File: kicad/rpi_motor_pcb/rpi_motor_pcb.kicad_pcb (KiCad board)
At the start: 2 copper layers, 65 x 84.5 mm, 16 parts, among them J1 Raspberry_Pi_2_3, J10 I2C, J11 LIM_SW, J2 Motor Z1, J3 Motor Z2, J4 PWR IN, J5 Motor X, J6 Motor Y, J7 Motor Z3, J8 I2C, J9 I2C

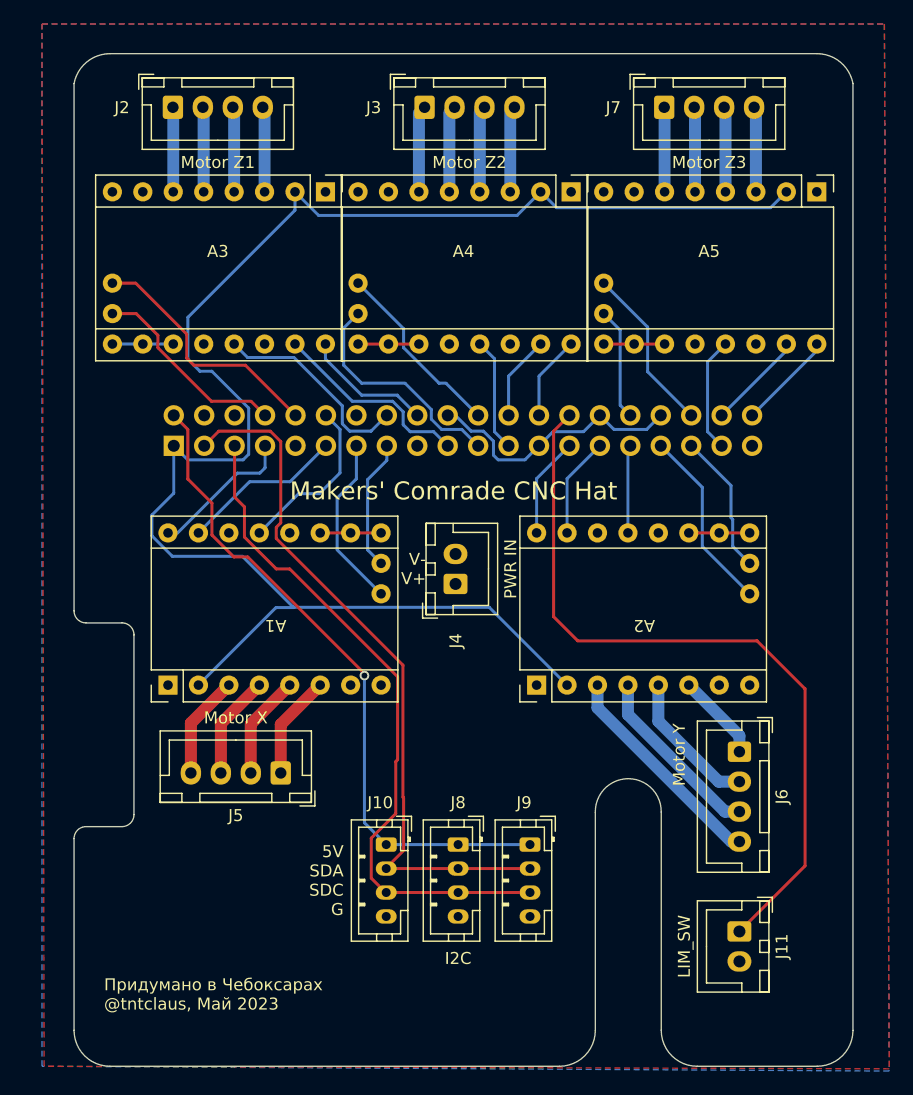
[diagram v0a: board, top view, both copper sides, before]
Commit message: rpi_motor_pcb: 6-axis canbus version
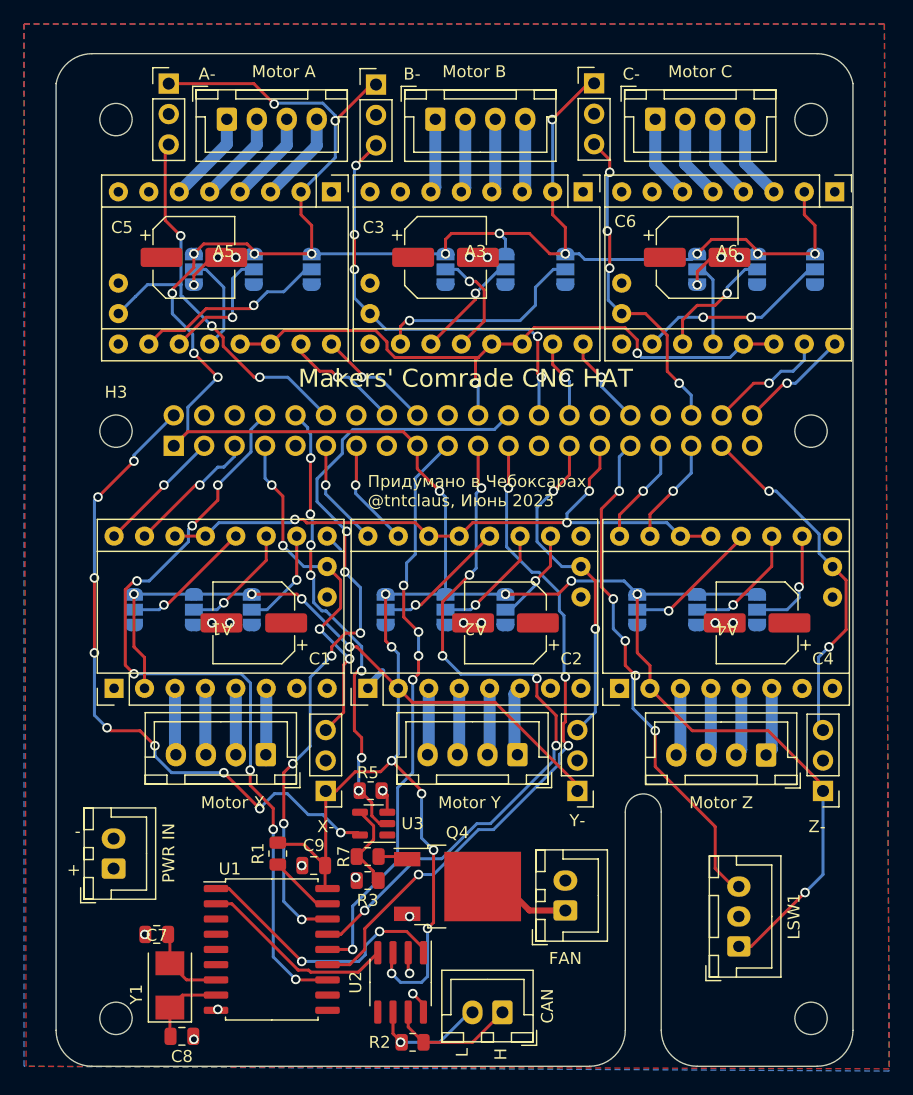
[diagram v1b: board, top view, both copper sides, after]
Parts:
- added A6: Motor C Driver, TMCSockets:TMC220X, F.Cu at (79.0, 33.5)
- added C1: 100µF 50V, Capacitor_SMD:CP_Elec_6.3x7.7, F.Cu at (39.5, 63.0)
- added C2: 100µF 50V, Capacitor_SMD:CP_Elec_6.3x7.7, F.Cu at (60.5, 63.0)
- added C3: 100µF 50V, Capacitor_SMD:CP_Elec_6.3x7.7, F.Cu at (55.5, 32.5)
- added C4: 100µF 50V, Capacitor_SMD:CP_Elec_6.3x7.7, F.Cu at (81.5, 63.0)
- added C5: 100µF 50V, Capacitor_SMD:CP_Elec_6.3x7.7, F.Cu at (34.5, 32.5)
- added C6: 100µF 50V, Capacitor_SMD:CP_Elec_6.3x7.7, F.Cu at (76.5, 32.5)
- added C7: 22pF, Capacitor_SMD:C_0805_2012Metric, F.Cu at (31.4, 89.0)
- added C8: 22pF, Capacitor_SMD:C_0805_2012Metric, F.Cu at (33.5, 97.5)
- added C9: 0.1µF, Capacitor_SMD:C_0805_2012Metric, F.Cu at (44.5, 83.2)
- added H1: MountingHole, MountingHole:MountingHole_2.7mm_M2.5_ISO14580, F.Cu at (28.0, 96.0)
- added H2: MountingHole, MountingHole:MountingHole_2.7mm_M2.5_ISO14580, F.Cu at (86.0, 96.0)
- added H3: MountingHole, MountingHole:MountingHole_2.7mm_M2.5_ISO14580, F.Cu at (28.0, 47.0)
- added H4: MountingHole, MountingHole:MountingHole_2.7mm_M2.5_ISO14580, F.Cu at (86.0, 47.0)
- added H5: MountingHole, MountingHole:MountingHole_2.7mm_M2.5_ISO14580, F.Cu at (28.0, 21.0)
- added H6: MountingHole, MountingHole:MountingHole_2.7mm_M2.5_ISO14580, F.Cu at (86.0, 21.0)
- added J12: Motor C, Connector_JST:JST_XH_B4B-XH-A_1x04_P2.50mm_Vertical, F.Cu at (73.0, 21.0)
- added J13: B-, Connector_PinHeader_2.54mm:PinHeader_1x03_P2.54mm_Vertical, F.Cu at (49.7, 18.1)
- added J14: C-, Connector_PinHeader_2.54mm:PinHeader_1x03_P2.54mm_Vertical, F.Cu at (67.9, 18.0)
- added J15: Y-, Connector_PinHeader_2.54mm:PinHeader_1x03_P2.54mm_Vertical, F.Cu at (66.5, 77.0)
- added J16: Z-, Connector_PinHeader_2.54mm:PinHeader_1x03_P2.54mm_Vertical, F.Cu at (87.0, 77.0)
- added J18: FAN, Connector_JST:JST_XH_B2B-XH-A_1x02_P2.50mm_Vertical, F.Cu at (65.5, 87.0)
- added JP1: MS3, Jumper:SolderJumper-3_P1.3mm_Open_RoundedPad1.0x1.5mm, B.Cu at (29.5, 61.9)
- added JP10: MS3, Jumper:SolderJumper-3_P1.3mm_Open_RoundedPad1.0x1.5mm, B.Cu at (71.5, 61.9)
- added JP11: MS2, Jumper:SolderJumper-3_P1.3mm_Open_RoundedPad1.0x1.5mm, B.Cu at (76.5, 61.9)
- added JP12: MS1, Jumper:SolderJumper-3_P1.3mm_Open_RoundedPad1.0x1.5mm, B.Cu at (81.5, 61.9)
- added JP13: MS3, Jumper:SolderJumper-3_P1.3mm_Open_RoundedPad1.0x1.5mm, B.Cu at (34.5, 33.5)
- added JP14: MS2, Jumper:SolderJumper-3_P1.3mm_Open_RoundedPad1.0x1.5mm, B.Cu at (39.5, 33.5)
- added JP15: MS1, Jumper:SolderJumper-3_P1.3mm_Open_RoundedPad1.0x1.5mm, B.Cu at (44.3, 33.5)
- added JP16: MS3, Jumper:SolderJumper-3_P1.3mm_Open_RoundedPad1.0x1.5mm, B.Cu at (76.5, 33.5)
- added JP17: MS2, Jumper:SolderJumper-3_P1.3mm_Open_RoundedPad1.0x1.5mm, B.Cu at (81.5, 33.5)
- added JP18: MS1, Jumper:SolderJumper-3_P1.3mm_Open_RoundedPad1.0x1.5mm, B.Cu at (86.3, 33.5)
- added JP2: MS2, Jumper:SolderJumper-3_P1.3mm_Open_RoundedPad1.0x1.5mm, B.Cu at (34.5, 61.9)
- added JP3: MS1, Jumper:SolderJumper-3_P1.3mm_Open_RoundedPad1.0x1.5mm, B.Cu at (39.3, 61.9)
- added JP4: MS3, Jumper:SolderJumper-3_P1.3mm_Open_RoundedPad1.0x1.5mm, B.Cu at (50.5, 61.9)
- added JP5: MS2, Jumper:SolderJumper-3_P1.3mm_Open_RoundedPad1.0x1.5mm, B.Cu at (55.5, 61.9)
- added JP6: MS1, Jumper:SolderJumper-3_P1.3mm_Open_RoundedPad1.0x1.5mm, B.Cu at (60.5, 61.9)
- added JP7: MS3, Jumper:SolderJumper-3_P1.3mm_Open_RoundedPad1.0x1.5mm, B.Cu at (55.5, 33.5)
- added JP8: MS2, Jumper:SolderJumper-3_P1.3mm_Open_RoundedPad1.0x1.5mm, B.Cu at (60.5, 33.5)
- added JP9: MS1, Jumper:SolderJumper-3_P1.3mm_Open_RoundedPad1.0x1.5mm, B.Cu at (65.5, 33.5)
- added Q4: HY1403D, Package_TO_SOT_SMD:TO-252-2, F.Cu at (56.5, 85.0)
- added R1: 10k, Resistor_SMD:R_0805_2012Metric, F.Cu at (41.5, 82.2)
- added R2: 120, Resistor_SMD:R_0805_2012Metric, F.Cu at (52.8, 98.0)
- added R3: 10k, Resistor_SMD:R_0805_2012Metric, F.Cu at (49.0, 84.5)
- added R5: 10k, Resistor_SMD:R_0805_2012Metric, F.Cu at (49.2, 77.0)
- added R7: 10k, Resistor_SMD:R_0805_2012Metric, F.Cu at (49.0, 82.5)
- added U1: MCP2515-xSO, Package_SO:SOIC-18W_7.5x11.6mm_P1.27mm, F.Cu at (41.0, 90.2)
- added U2: SN65HVD230, Package_SO:SOIC-8_3.9x4.9mm_P1.27mm, F.Cu at (51.8, 93.0)
- added U3: 74LVC1G17, Package_TO_SOT_SMD:SOT-23-5, F.Cu at (49.5, 79.8)
- added Y1: Crystal, Crystal:Crystal_SMD_5032-2Pin_5.0x3.2mm, F.Cu at (32.5, 93.2)
- A1: value MKS_TMC2209 Motor X -> Motor X Driver
- A2: value MKS_TMC2209 Motor Y -> Motor Y Driver
- A3: value MKS_TMC2209 Motor Z1 -> Motor B Driver
- A4: value MKS_TMC2209 Motor Z2 -> Motor Z Driver
- A5: value MKS_TMC2209 Motor Z3 -> Motor A Driver
- J10: value I2C -> CAN; footprint Connector_JST:JST_PH_B4B-PH-K_1x04_P2.00mm_Vertical -> Connector_JST:JST_XH_B2B-XH-A_1x02_P2.50mm_Vertical
- J11: value LIM_SW -> A-; footprint Connector_JST:JST_XH_B2B-XH-A_1x02_P2.50mm_Vertical -> Connector_PinHeader_2.54mm:PinHeader_1x03_P2.54mm_Vertical
- J2: value Motor Z1 -> Motor Y
- J3: value Motor Z2 -> Motor B
- J6: value Motor Y -> Motor Z
- J7: value Motor Z3 -> Motor A
- J8: value I2C -> X-; footprint Connector_JST:JST_PH_B4B-PH-K_1x04_P2.00mm_Vertical -> Connector_PinHeader_2.54mm:PinHeader_1x03_P2.54mm_Vertical
- J9: value I2C -> LSW1; footprint Connector_JST:JST_PH_B4B-PH-K_1x04_P2.00mm_Vertical -> Connector_JST:JST_XH_B3B-XH-A_1x03_P2.50mm_Vertical
- moved J11 85.3 mm to (32.4, 18.0), turned to 0 degrees
- moved J2 61.2 mm to (61.5, 74.0), turned to 180 degrees
- moved A5 40.5 mm to (37.0, 33.5)
- moved J4 37.1 mm to (27.8, 83.5)
- moved J7 36.5 mm to (37.2, 21.0)
- moved A4 36.0 mm to (79.0, 62.0), turned to 90 degrees
- moved A3 21.5 mm to (58.0, 33.5)
- moved J9 19.4 mm to (80.0, 90.0), turned to 90 degrees
- moved J10 17.0 mm to (60.2, 95.5), turned to 180 degrees
- moved A2 14.1 mm to (58.0, 62.0)
- moved J8 11.9 mm to (45.5, 77.0), turned to 180 degrees
- moved A1 4.51 mm to (36.8, 62.0)
- moved J6 2.24 mm to (82.2, 74.0), turned to 180 degrees
- moved J5 1.97 mm to (40.5, 74.0)
- moved J3 1.35 mm to (54.6, 21.0)
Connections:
- net /Motor Z3/1A renamed /Motor A/1A
- net /Motor Z3/1B renamed /Motor A/1B
- net /Motor Z3/2A renamed /Motor A/2A
- net /Motor Z3/2B renamed /Motor A/2B
- A1 pad 10: GND -> /Motor X/MS1
- A1 pad 11: GND -> /Motor X/MS2
- A1 pad 12: unconnected-(A1-Pad12) -> /Motor X/MS3
- A1 pad 13: /MotX UART -> /UART_X
- A1 pad 14: unconnected-(A1-Pad14) -> /UART_X
- A1 pad 15: /MotX STEP -> /MX STEP
- A1 pad 16: /MotX DIR -> /MX DIR
- A1 pad 17: /MotX DIAG -> /MX DIAG
- A1 pad 18: /MotX INDEX -> unconnected-(A1-Pad18)
- A2 pad 10: GND -> /Motor Y/MS1
- A2 pad 11: GND -> /Motor Y/MS2
- A2 pad 12: unconnected-(A2-Pad12) -> /Motor Y/MS3
- A2 pad 13: /MotY UART -> /UART_X
- A2 pad 14: unconnected-(A2-Pad14) -> /UART_X
- A2 pad 15: /MotY STEP -> /MY STEP
- A2 pad 16: /MotY DIR -> /MY DIR
- A2 pad 17: /MotY DIAG -> /MY DIAG
- A2 pad 18: /MotY INDEX -> unconnected-(A2-Pad18)
- A3 pad 10: GND -> /Motor B/MS1
- A3 pad 11: GND -> /Motor B/MS2
- A3 pad 12: unconnected-(A3-Pad12) -> /Motor B/MS3
- A3 pad 13: /MotZ1 UART -> /UART_A
- A3 pad 14: unconnected-(A3-Pad14) -> /UART_A
- A3 pad 15: /MotZ1 STEP -> /MB STEP
- A3 pad 16: /MotZ1 DIR -> /MB DIR
- A3 pad 17: /MotZ1 DIAG -> /MB DIAG
- A3 pad 18: /MotZ1 INDEX -> unconnected-(A3-Pad18)
- A3 pad 3: /Motor Z1/1B -> /Motor B/1B
- A3 pad 4: /Motor Z1/1A -> /Motor B/1A
- A3 pad 5: /Motor Z1/2A -> /Motor B/2A
- A3 pad 6: /Motor Z1/2B -> /Motor B/2B
- A4 pad 10: GND -> /Motor Z/MS1
- A4 pad 11: GND -> /Motor Z/MS2
- A4 pad 12: unconnected-(A4-Pad12) -> /Motor Z/MS3
- A4 pad 13: /MotZ2 UART -> /UART_X
- A4 pad 14: unconnected-(A4-Pad14) -> /UART_X
- A4 pad 15: /MotZ2 STEP -> /MZ STEP
- A4 pad 16: /MotZ2 DIR -> /MZ DIR
- A4 pad 17: /MotZ2 DIAG -> /MZ DIAG
- A4 pad 18: /MotZ2 INDEX -> unconnected-(A4-Pad18)
- A4 pad 3: /Motor Z2/1B -> /Motor Z/1B
- A4 pad 4: /Motor Z2/1A -> /Motor Z/1A
- A4 pad 5: /Motor Z2/2A -> /Motor Z/2A
- A4 pad 6: /Motor Z2/2B -> /Motor Z/2B
- A5 pad 10: GND -> /Motor A/MS1
- A5 pad 11: GND -> /Motor A/MS2
- A5 pad 12: unconnected-(A5-Pad12) -> /Motor A/MS3
- A5 pad 13: /MotZ3 UART -> /UART_A
- A5 pad 14: unconnected-(A5-Pad14) -> /UART_A
- A5 pad 15: /MotZ3 STEP -> /MA STEP
- A5 pad 16: /MotZ3 DIR -> /MA DIR
- A5 pad 17: /MotZ3 DIAG -> /MA DIAG
- A5 pad 18: /MotZ3 INDEX -> unconnected-(A5-Pad18)
- J1 pad 10: /MotZ1 INDEX -> /FAN
- J1 pad 11: /MotX STEP -> /MY DIR
- J1 pad 12: /MotX UART -> /MA DIAG
- J1 pad 13: /MotX INDEX -> /MY STEP
- J1 pad 15: /MotX DIAG -> unconnected-(J1-Pad15)
- J1 pad 16: /MotZ1 UART -> /MA STEP
- J1 pad 17: unconnected-(J1-Pad17) -> +3V3
- J1 pad 18: /MotZ1 DIR -> /MA DIR
- J1 pad 19: /MotZ1 STEP -> /CAN_MOSI
- J1 pad 2: +5V -> VCC
- J1 pad 21: /MotZ2 DIAG -> /CAN_MISO
- J1 pad 22: /MotZ2 INDEX -> /UART_A
- J1 pad 23: /MotZ2 UART -> /CAN_SCK
- J1 pad 24: /MotZ2 STEP -> /CAN_CS
- J1 pad 26: /MotZ2 DIR -> /MB DIAG
- J1 pad 27: /MotY DIR -> /MY DIAG
- J1 pad 28: /LIM_SW1 -> /MB STEP
- J1 pad 29: /MotY STEP -> /UART_X
- J1 pad 3: /SDA -> /MX DIR
- J1 pad 31: /MotY UART -> /LIM_SW1
- J1 pad 32: /MotZ3 DIAG -> /MB DIR
- J1 pad 33: /MotY INDEX -> /MZ DIR
- J1 pad 35: /MotY DIAG -> /MZ STEP
- J1 pad 36: /MotZ3 INDEX -> /MC DIAG
- J1 pad 37: /MotZ3 UART -> /MZ DIAG
- J1 pad 38: /MotZ3 STEP -> /MC STEP
- J1 pad 40: /MotZ3 DIR -> /MC DIR
- J1 pad 5: /SDC -> /MX STEP
- J1 pad 7: /MotX DIR -> /MX DIAG
- J1 pad 8: /MotZ1 DIAG -> /CAN_INT
- J10 pad 1: +5V -> /CAN/H
- J10 pad 2: /SDA -> /CAN/L
- J11 pad 1: /LIM_SW1 -> +3V3
- J2 pad 1: /Motor Z1/2B -> /Motor Y/2B
- J2 pad 2: /Motor Z1/2A -> /Motor Y/2A
- J2 pad 3: /Motor Z1/1A -> /Motor Y/1A
- J2 pad 4: /Motor Z1/1B -> /Motor Y/1B
- J3 pad 1: /Motor Z2/2B -> /Motor B/2B
- J3 pad 2: /Motor Z2/2A -> /Motor B/2A
- J3 pad 3: /Motor Z2/1A -> /Motor B/1A
- J3 pad 4: /Motor Z2/1B -> /Motor B/1B
- J6 pad 1: /Motor Y/2B -> /Motor Z/2B
- J6 pad 2: /Motor Y/2A -> /Motor Z/2A
- J6 pad 3: /Motor Y/1A -> /Motor Z/1A
- J6 pad 4: /Motor Y/1B -> /Motor Z/1B
- J8 pad 1: +5V -> +3V3
- J8 pad 2: /SDA -> GND
- J8 pad 3: /SDC -> /MX DIAG
- J9 pad 1: +5V -> +3V3
- J9 pad 2: /SDA -> GND
- J9 pad 3: /SDC -> /LIM_SW1
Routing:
- net +3V3: track 137.7 -> 353.6 mm, vias 0 -> 31
- net /CAN_INT: track 0.00 -> 66.5 mm, vias 0 -> 7
- net /CAN_CS: track 0.00 -> 63.4 mm, vias 0 -> 7
- net /CAN_MISO: track 0.00 -> 60.1 mm, vias 0 -> 6
- net /SDA: track 60.0 -> 0.00 mm
- net /SDC: track 57.0 -> 0.00 mm
- net /CAN_SCK: track 0.00 -> 56.9 mm, vias 0 -> 4
- net +5V: track 55.8 -> 0.00 mm, vias 1 -> 0
- net VCC: track 0.00 -> 55.6 mm, vias 0 -> 9
- net /UART_A: track 0.00 -> 54.7 mm, vias 0 -> 2
- net /UART_X: track 0.00 -> 54.4 mm, vias 0 -> 3
- net /CAN_MOSI: track 0.00 -> 48.4 mm, vias 0 -> 5
- net /FAN: track 0.00 -> 38.4 mm, vias 0 -> 7
- net /MB DIAG: track 0.00 -> 36.9 mm, vias 0 -> 5
- net /MA DIAG: track 0.00 -> 36.2 mm, vias 0 -> 3
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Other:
- board size 65 x 84.5 mm -> 66.5 x 84.5 mm
- board text added: "- +"
- board text added: "H"
- board text added: "L"
- board text added: "L H"
- board text added: "Makers' Comrade CNC HAT"
- board text added: "Придумано в Чебоксарах @tntclaus, Июнь 2023"
- board text removed: "5V SDA SDC G"
- board text removed: "Makers' Comrade CNC Hat"
- board text removed: "V- V+"
- board text removed: "Придумано в Чебоксарах @tntclaus, Май 2023"

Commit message: rpi_motor_pcb: 6-axis fix diag pin, add en pin
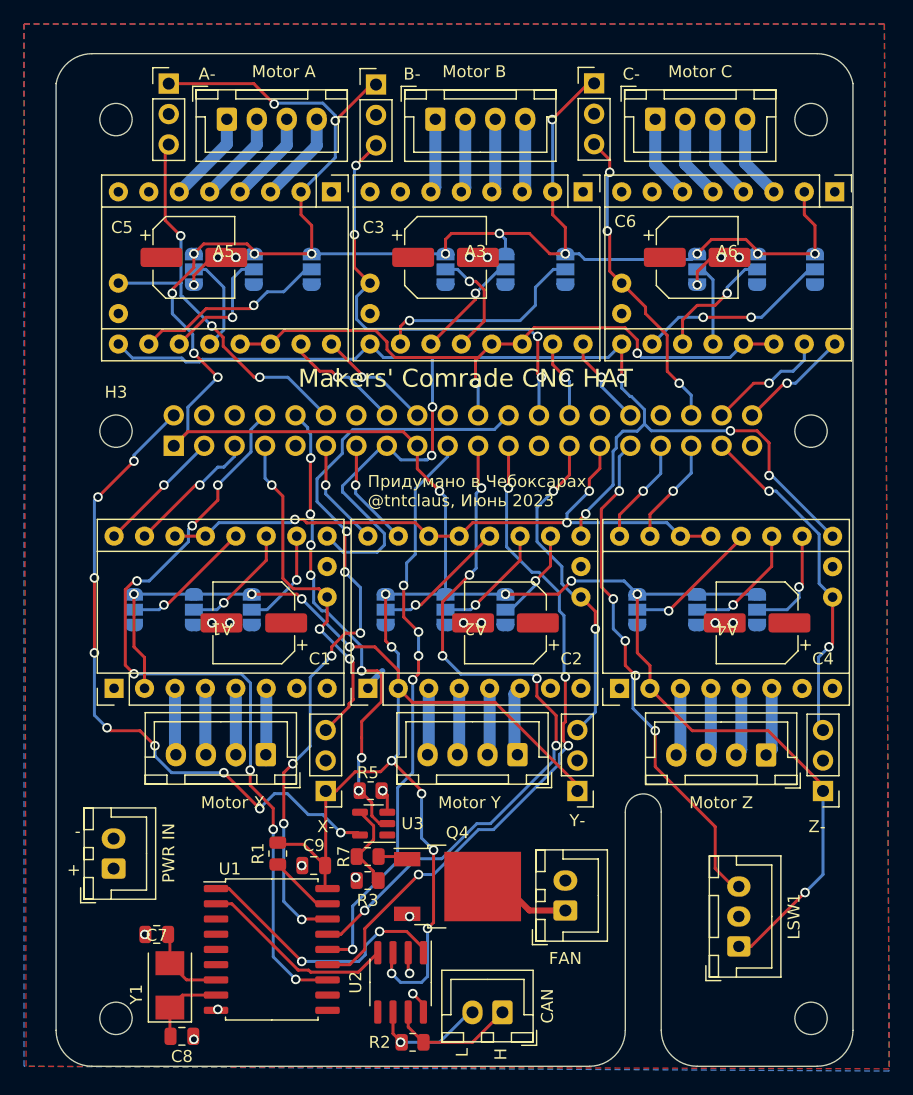
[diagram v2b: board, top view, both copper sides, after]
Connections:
- net VCC renamed +5V
- A1 pad 17: /MX DIAG -> unconnected-(A1-Pad17)
- A1 pad 18: unconnected-(A1-Pad18) -> /MX DIAG
- A1 pad 9: GND -> MEN
- A2 pad 17: /MY DIAG -> unconnected-(A2-Pad17)
- A2 pad 18: unconnected-(A2-Pad18) -> /MY DIAG
- A2 pad 9: GND -> MEN
- A3 pad 17: /MB DIAG -> unconnected-(A3-Pad17)
- A3 pad 18: unconnected-(A3-Pad18) -> /MB DIAG
- A3 pad 9: GND -> MEN
- A4 pad 17: /MZ DIAG -> unconnected-(A4-Pad17)
- A4 pad 18: unconnected-(A4-Pad18) -> /MZ DIAG
- A4 pad 9: GND -> MEN
- A5 pad 17: /MA DIAG -> unconnected-(A5-Pad17)
- A5 pad 18: unconnected-(A5-Pad18) -> /MA DIAG
- A5 pad 9: GND -> MEN
- A6 pad 17: /MC DIAG -> unconnected-(A6-Pad17)
- A6 pad 18: unconnected-(A6-Pad18) -> /MC DIAG
- A6 pad 9: GND -> MEN
- J1 pad 15: unconnected-(J1-Pad15) -> MEN
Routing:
- net MEN: track 0.00 -> 114.8 mm, vias 0 -> 6
- net /MB DIAG: track 36.9 -> 38.8 mm, vias 5 -> 4
- net /FAN: track 38.4 -> 40.2 mm
- net GND: track 17.2 -> 15.6 mm
- net /MC DIAG: track 27.4 -> 26.1 mm, vias 4 -> 3
- net /MA DIAG: track 36.2 -> 35.2 mm
- net /MZ DIAG: track 29.6 -> 28.6 mm
- net +3V3: track 353.6 -> 354.5 mm
- net /MY DIAG: track 28.4 -> 27.8 mm
- net /MX DIAG: track 30.1 -> 29.6 mm, vias 4 -> 3

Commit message: rpi_motor_pcb: 7-axis canbus version (removed useless fan and limit switch)
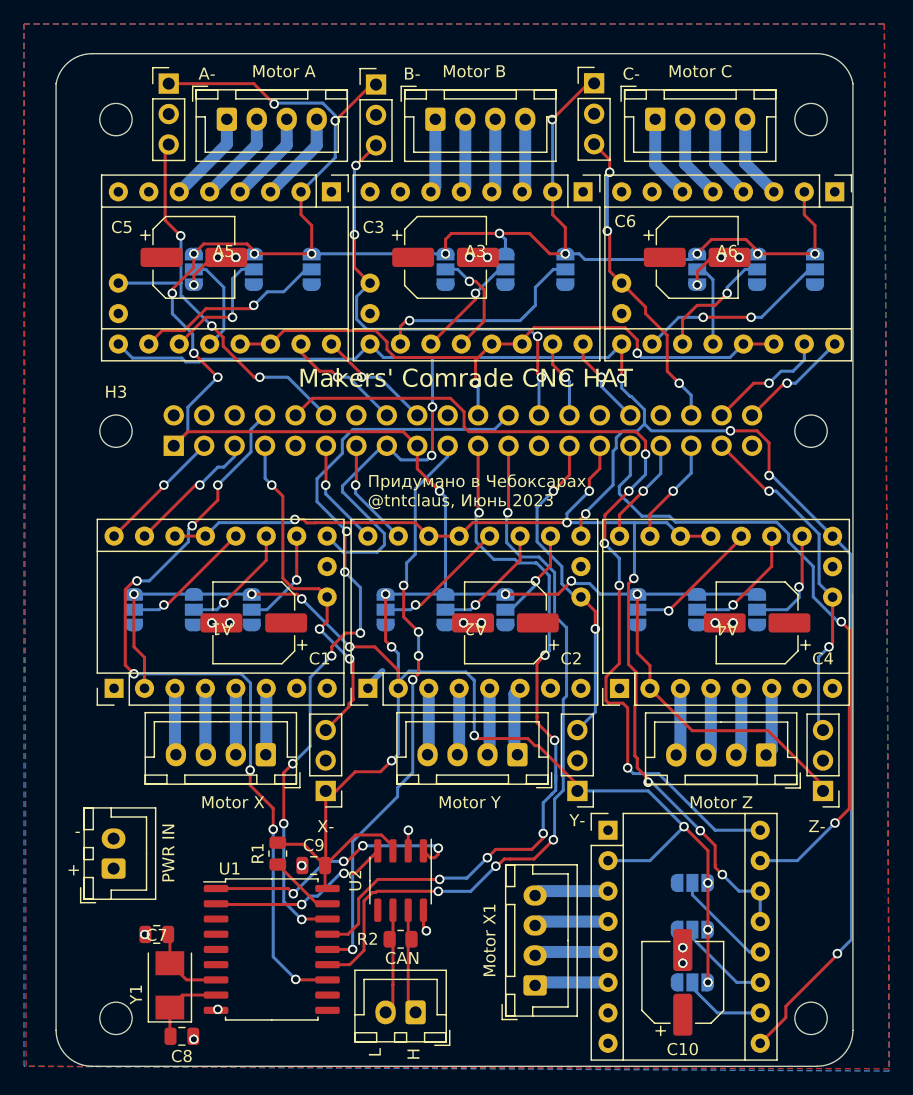
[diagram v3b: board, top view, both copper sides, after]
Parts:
- removed J18: FAN, Connector_JST:JST_XH_B2B-XH-A_1x02_P2.50mm_Vertical
- removed Q4: HY1403D, Package_TO_SOT_SMD:TO-252-2
- removed R3, R5, R7: 10k, Resistor_SMD:R_0805_2012Metric
- removed U3: 74LVC1G17, Package_TO_SOT_SMD:SOT-23-5
- added A7: Motor X1 Driver, TMCSockets:TMC2208, F.Cu at (76.2, 89.4)
- added C10: 100µF 50V, Capacitor_SMD:CP_Elec_6.3x7.7, F.Cu at (75.3, 93.0)
- added JP19: MS3, Jumper:SolderJumper-3_P1.3mm_Open_RoundedPad1.0x1.5mm, B.Cu at (76.1, 84.7)
- added JP20: MS2, Jumper:SolderJumper-3_P1.3mm_Open_RoundedPad1.0x1.5mm, B.Cu at (76.1, 88.6)
- added JP21: MS1, Jumper:SolderJumper-3_P1.3mm_Open_RoundedPad1.0x1.5mm, B.Cu at (76.1, 93.0)
- J9: value LSW1 -> Motor X1; footprint Connector_JST:JST_XH_B3B-XH-A_1x03_P2.50mm_Vertical -> Connector_JST:JST_XH_B4B-XH-A_1x04_P2.50mm_Vertical
- moved J9 17.3 mm to (63.0, 93.2)
- moved R2 8.66 mm to (51.8, 89.4)
- moved U2 8.50 mm to (51.8, 84.5)
- moved J10 7.25 mm to (53.0, 95.5)
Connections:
- J1 pad 10: /FAN -> /MX1 DIR
- J1 pad 31: /LIM_SW1 -> /MX1 STEP
- J9 pad 1: +3V3 -> /Motor X1/2B
- J9 pad 2: GND -> /Motor X1/2A
- J9 pad 3: /LIM_SW1 -> /Motor X1/1A
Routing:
- net /MX1 DIR: track 0.00 -> 76.3 mm, vias 0 -> 5
- net +5V: track 55.6 -> 0.00 mm, vias 9 -> 0
- net /MX1 STEP: track 0.00 -> 54.3 mm, vias 0 -> 2
- net MEN: track 114.8 -> 160.9 mm, vias 6 -> 7
- net /LIM_SW1: track 43.0 -> 0.00 mm, vias 5 -> 0
- net /FAN: track 40.2 -> 0.00 mm, vias 7 -> 0
- net /UART_X: track 54.4 -> 93.7 mm, vias 3 -> 7
- net /Motor X1/MS3: track 0.00 -> 8.63 mm
- net Net-(R3-Pad1): track 7.91 -> 0.00 mm
- net /Motor X1/MS2: track 0.00 -> 7.89 mm
- net Net-(J18-Pad1): track 7.73 -> 0.00 mm
- net /Motor X1/MS1: track 0.00 -> 6.98 mm
- net /Motor X1/1B: track 0.00 -> 6.24 mm
- net /Motor X1/1A: track 0.00 -> 6.22 mm
- net /Motor X1/2A: track 0.00 -> 6.20 mm
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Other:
- outline, holes or cut-outs redrawn
